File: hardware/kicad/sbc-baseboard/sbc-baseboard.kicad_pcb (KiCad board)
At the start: 6 copper layers, 140 x 100 mm, 339 parts, among them J1 USB-C upstream, J10 RJ45 magjack 10/100, J11 COM/NO/NC, J12 COM/NO/NC, J13 Console, J14 +5V_TGT out, J15 GPIO + I2C, J16 SWD, J17 Qwiic PD, J18 PSU in (isolated), J19 PSU out (isolated), J2 USB-C PD in, J3 USB-C HID to target, J4 USB-A x2, J5 USB-A x2, J601 SWD (K20), J9 FTDI header, K801 G6K-2F-Y DC5, K802 G6K-2F-Y DC5, K803 JW1FSN-DC5V, Q101 2N7002, Q102 2N7002, Q801 2N7002, Q802 2N7002, Q803 AO3400A, SW201 RESET, SW601 DAP RESET, U101 STUSB4500QTR, U102 PCA9517A, U103 TPS54560BDDA, U104 TPS54560BDDA, U105 TPS62823DLC, U201 MK64FN1M0VLL12, U202 USBLC6-2SC6, U301 KSZ8081RNA, U401 USBLC6-2SC6, U402 USB2517, U403 TPS2553DBV, U404 TPS2553DBV, U405 TPS2553DBV, U406 TPS2553DBV, U407 TPS2553DBV, U408 USBLC6-2SC6, U409 USBLC6-2SC6, U410 USBLC6-2SC6, U411 USBLC6-2SC6, U501 FT231XS, U601 MK20DX128VFM5, U701 TXB0104PW, U702 TXB0108PW, U703 TXS0102DCU, U704 TPS26630RGE, U801 LTV-817, Y201 32.768kHz, Y301 25MHz, Y401 24MHz, Y601 8MHz

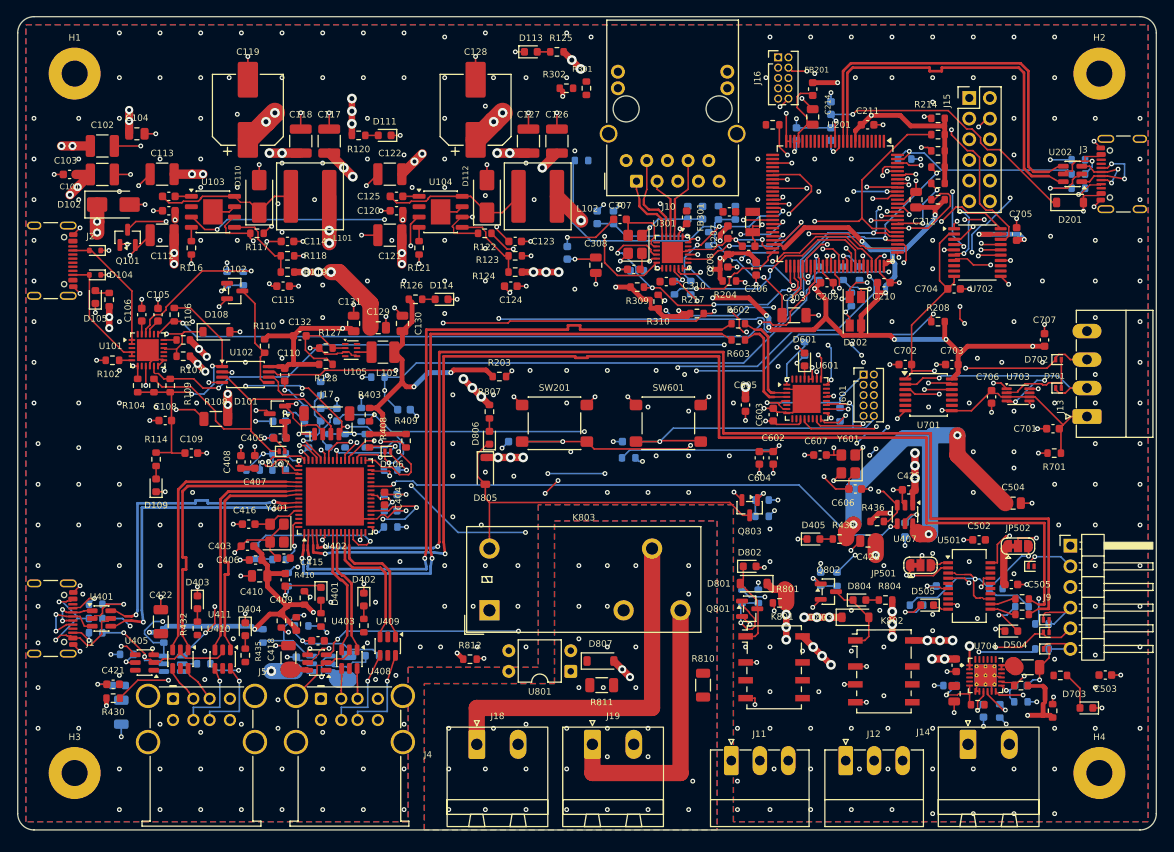
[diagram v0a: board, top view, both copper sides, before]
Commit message: The documents, the block diagram and the placed board for the barrel-jack inlet; 100 uF of bulk at the inlet
The specification (block diagram, connectors, parts, power tree and
budget at 20 W, pin budget, open questions, current pathways), the
README and the block diagram, the layout directives, guidelines and
reference-design review, the KiCad README and the protocol describe the
barrel inlet, the one +5V rail and the 3 A target rail; the PD inlet,
its controller, header and buffer and the two bucks remain as dated
history. A 100 uF electrolytic joins the two 47 uF at the inlet: the
hub's downstream ports want 120 uF on their rail, which buck 1's 194 uF
had given. Three older contradictions in the specification are settled
from the generator and the BOM: one FET per relay coil (2N7002 for the
signal relays, AO3400A for the power relay), the DAPLink on hub port 1,
the USB-A ports on hub ports 4 to 7. The board is committed placed and
unrouted (the route was stopped at the owner's request before it
finished): 271 parts, 480 connections, DRC clean.

Co-Authored-By: Claude Fable 5.1 <noreply@anthropic.com>
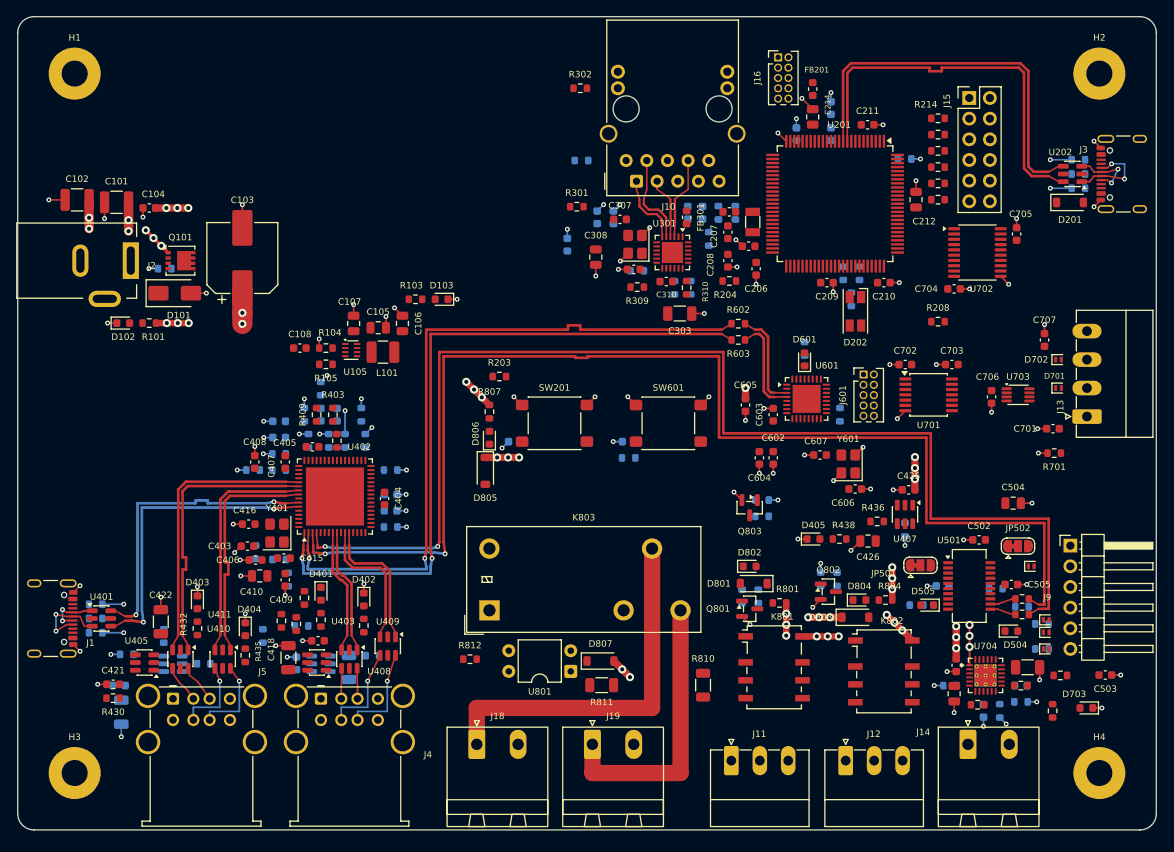
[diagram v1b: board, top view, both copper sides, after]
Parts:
- removed C109, C110: 100n, C_0603_1608Metric
- removed C111, C116: 100n/50V, C_0603_1608Metric
- removed C112, C113: 10u/50V, C_1210_3225Metric
- removed C114: 47p, C_0603_1608Metric
- removed C115: 4n7, C_0603_1608Metric
- removed C117, C118: 47u/10V, C_1210_3225Metric
- removed C119: 100u/10V, CP_Elec_8x10.5
- removed C129: 10u, C_0805_2012Metric
- removed C130, C131: 22u, C_0805_2012Metric
- removed C132: 120p, C_0603_1608Metric
- removed the C212 at (110.5, 22.5)
- removed the C213 at (95.8, 14.4)
- removed the C214 at (97.8, 12.3)
- removed the C301 at (82.4, 24.1)
- removed the C302 at (84.2, 24.1)
- removed the C303 at (95.5, 36.7)
- removed the C304 at (73.2, 24.7)
- removed the C305 at (71.2, 24.7)
- removed the C306 at (75.8, 31.1)
- removed D104: ESDA25W, D_SOD-523
- removed D105, D109, D111, D113, D114: LED AMBER, LED_0603_1608Metric
- removed D106, D107: PESD5V0S1UL, D_SOD-882
- removed D108: BZT52C5V1, D_SOD-123
- removed D110, D112: B560C, D_SMA
- removed the J15 at (117.0, 10.0)
- removed J17: Qwiic PD, JST_SH_BM04B-SRSS-TB_1x04-1MP_P1.00mm_Vertical
- removed the J3 at (136.9, 19.3)
- removed L102: 10u/6A, L_Coilcraft_XAL7020-102
- removed L103: 470n/4A, L_1210_3225Metric
- removed Q102: 2N7002, SOT-23
- removed R106, R109, R110: 10k, R_0603_1608Metric
- removed R107, R111, R112, R113, R115, R127: 100k, R_0603_1608Metric
- removed R108: 470, R_1206_3216Metric
- removed R114, R126: 470, R_0603_1608Metric
- removed R116, R121: 243k, R_0603_1608Metric
- removed R117, R122: 16.9k, R_0603_1608Metric
- removed R118, R123: 9.76k, R_0603_1608Metric
- removed R119, R124: 51.1k, R_0603_1608Metric
- removed R120, R125: 1k, R_0603_1608Metric
- removed R128: 453k, R_0603_1608Metric
- removed the R204 at (87.5, 32.5)
- removed R217, R218: 4.7k, R_0603_1608Metric
- removed the R307 at (80.8, 33.3)
- removed U101: STUSB4500QTR, QFN-24-1EP_4x4mm_P0.5mm_EP2.7x2.7mm
- removed U102: PCA9517A, TSSOP-8_4.4x3mm_P0.65mm
- removed U103, U104: TPS54560BDDA, HSOP-8-1EP_3.9x4.9mm_P1.27mm_EP2.41x3.1mm
- added D401: LED GREEN, LED_0603_1608Metric, F.Cu at (37.3, 71.0)
- added D805: 1N4148W, D_SOD-123, F.Cu at (57.5, 55.9)
- added J13: Console, PhoenixContact_MC_1,5_4-G-3.5_1x04_P3.50mm_Horizontal, F.Cu at (131.5, 49.2)
- added JP501: RTS/DTR, SolderJumper-3_P1.3mm_Bridged12_RoundedPad1.0x1.5mm, F.Cu at (111.0, 67.5)
- C101, C102: value 10u/50V -> 47u/10V
- C103: value 100n/50V -> 100u/10V; footprint C_0603_1608Metric -> CP_Elec_8x10.5
- C104: value 1u/50V -> 100n; footprint C_0805_2012Metric -> C_0603_1608Metric
- C105: value 1u -> 10u; footprint C_0603_1608Metric -> C_0805_2012Metric
- C106: value 1u -> 22u; footprint C_0603_1608Metric -> C_0805_2012Metric
- C107: value 1u -> 22u; footprint C_0603_1608Metric -> C_0805_2012Metric; moved to F.Cu
- C108: value 100n -> 120p
- C212: renamed from C120; value 100n/50V -> 10u; footprint C_0603_1608Metric -> C_0805_2012Metric
- C213: renamed from C121; value 10u/50V -> 100n; footprint C_1210_3225Metric -> C_0603_1608Metric; moved to B.Cu
- C214: renamed from C122; value 10u/50V -> 10u; footprint C_1210_3225Metric -> C_0805_2012Metric
- C301: renamed from C123; value 47p -> 100n; moved to B.Cu
- C302: renamed from C124; value 4n7 -> 100n; moved to B.Cu
- C303: renamed from C125; value 100n/50V -> 1n/2kV; footprint C_0603_1608Metric -> C_1206_3216Metric
- C304: renamed from C126; value 47u/10V -> 2u2; footprint C_1210_3225Metric -> C_0603_1608Metric; moved to B.Cu
- C305: renamed from C127; value 47u/10V -> 100n; footprint C_1210_3225Metric -> C_0603_1608Metric; moved to B.Cu
- C306: renamed from C128; value 100u/10V -> 22p; footprint CP_Elec_8x10.5 -> C_0603_1608Metric
- D101: value BAT54C -> SMAJ5.0A; footprint SOT-23 -> D_SMA
- D102: value SMAJ24A -> LED AMBER; footprint D_SMA -> LED_0603_1608Metric
- D103: value ESDA25W -> LED AMBER; footprint D_SOD-523 -> LED_0603_1608Metric
- J15: renamed from D805; value 1N4148W -> GPIO + I2C; footprint D_SOD-123 -> PinHeader_2x06_P2.54mm_Vertical
- J2: value USB-C PD in -> 5 V in, 2.5 mm; footprint USB_C_Receptacle_GCT_USB4105-xx-A_16P_TopMnt_Horizontal_PegClear -> BarrelJack_Kycon_KLDX-0202-xC_Horizontal
- J3: renamed from D401; value LED GREEN -> USB-C HID to target; footprint LED_0603_1608Metric -> USB_C_Receptacle_GCT_USB4105-xx-A_16P_TopMnt_Horizontal_PegClear
- L101: value 10u/6A -> 470n/4A; footprint L_Coilcraft_XAL7020-102 -> L_1210_3225Metric
- Q101: value 2N7002 -> DMP3013SFV; footprint SOT-23 -> Diodes_PowerDI3333-8
- R101: value 10k -> 1k
- R102: value 10k -> 100k; moved to B.Cu
- R103: value 1k -> 470
- R104: value 4.7k -> 100k
- R105: value 4.7k -> 453k
- R204: renamed from J13; value Console -> 10k; footprint PhoenixContact_MC_1,5_4-G-3.5_1x04_P3.50mm_Horizontal -> R_0603_1608Metric
- R307: renamed from JP501; value RTS/DTR -> 33; footprint SolderJumper-3_P1.3mm_Bridged12_RoundedPad1.0x1.5mm -> R_0603_1608Metric; moved to B.Cu
- R708: value 3.65k 1% -> 6.04k 1%
- moved J3 112.2 mm to (136.9, 19.3), turned to 90 degrees
- moved J15 75.1 mm to (117.0, 10.0), turned to 0 degrees
- moved C212 63.9 mm to (110.5, 22.5), turned to 90 degrees
- moved C214 52.5 mm to (97.8, 12.3), turned to 90 degrees
- moved C213 51.5 mm to (95.8, 14.4), turned to 90 degrees
- moved R204 47.0 mm to (87.5, 32.5), turned to 0 degrees
- moved R307 45.6 mm to (80.8, 33.3), turned to -90 degrees
- moved D103 43.0 mm to (52.1, 34.8)
- moved C303 37.7 mm to (81.4, 36.5), turned to 0 degrees
- moved C106 32.1 mm to (47.3, 37.7)
- moved R103 29.0 mm to (48.9, 34.8)
- moved C306 27.6 mm to (75.8, 31.1), turned to 180 degrees
- moved C105 27.1 mm to (44.3, 38.2), turned to 0 degrees
- moved C302 25.2 mm to (84.2, 24.1), turned to -90 degrees
- moved R104 23.6 mm to (37.9, 40.8), turned to 180 degrees
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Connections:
- net /Target I/O/+5V_TGT_OUT renamed /Target I/O/+5V_TGT
- C101 pad 1: VBUS_IN -> +5V
- C102 pad 1: VBUS_IN -> +5V
- C103 pad 1: VBUS_IN -> +5V
- C104 pad 1: VBUS_IN -> +5V
- C105 pad 1: Net-(U101-VREG_1V2) -> +5V
- C106 pad 1: Net-(U101-VREG_2V7) -> +3V3
- C107 pad 1: +3V3_PRG -> +3V3
- C108 pad 1: +3V3_PD -> +3V3
- C108 pad 2: GND -> Net-(U105-FB)
- C212 pad 1: VBUS_IN -> +3V3
- C213 pad 1: VBUS_IN -> +3V3A
- C214 pad 1: VBUS_IN -> +3V3A
- C301 pad 1: Net-(U104-COMP) -> Net-(J10-TCT)
- C302 pad 1: Net-(C124-Pad1) -> Net-(J10-RCT)
- C303 pad 1: Net-(U104-BOOT) -> Net-(C303-Pad1)
- C303 pad 2: Net-(D112-K) -> GND
- C304 pad 1: +5V_TGT -> Net-(U301-VDD_1.2)
- C305 pad 1: +5V_TGT -> Net-(U301-VDD_1.2)
- C306 pad 1: +5V_TGT -> Net-(U301-XO)
- C417 pad 1: +5V_PORTS -> +5V
- C419 pad 1: +5V_PORTS -> +5V
- C421 pad 1: +5V_PORTS -> +5V
- C423 pad 1: +5V_PORTS -> +5V
- C425 pad 1: +5V_PORTS -> +5V
- C605 pad 1: +5V_PORTS -> +5V
- C708 pad 1: +5V_TGT -> +5V
- C709 pad 1: +5V_TGT -> +5V
- D101 pad 1: +3V3 -> Net-(D101-K)
- D101 pad 2: +3V3_PRG -> GND
- D102 pad 1: VBUS_IN -> GND
- D102 pad 2: GND -> Net-(D102-A)
- D103 pad 2: Net-(D103-A2) -> Net-(D103-A)
- D801 pad 1: +5V_PORTS -> +5V
- D803 pad 1: +5V_PORTS -> +5V
- J15 pad 1: +5V_PORTS -> VREF_TGT
- J15 pad 2: Net-(D805-A) -> GND
- K801 pad 8: +5V_PORTS -> +5V
- K802 pad 8: +5V_PORTS -> +5V
- K803 pad 1: +5V_PORTS -> +5V
- L101 pad 1: Net-(D110-K) -> Net-(U105-SW)
- L101 pad 2: +5V_PORTS -> +3V3
- Q101 pad 1: /Power/PD_EN_GATE -> +5V
- Q101 pad 2: GND -> +5V
- Q101 pad 3: /Power/BUCK_EN -> +5V
- R101 pad 1: VBUS_IN -> +5V
- R101 pad 2: Net-(D105-A) -> Net-(D102-A)
- R102 pad 1: Net-(U101-RESET) -> Net-(Q101-G)
- R103 pad 1: Net-(U101-VBUS_VS_DISCH) -> +3V3
- R103 pad 2: VBUS_IN -> Net-(D103-A)
- R104 pad 1: +3V3_PD -> Net-(U105-FB)
- R104 pad 2: /Power/PD_SCL -> GND
- R105 pad 1: +3V3_PD -> +3V3
- R105 pad 2: /Power/PD_SDA -> Net-(U105-FB)
- R204 pad 1: VREF_TGT -> +3V3
- R204 pad 2: Net-(D701-K) -> Net-(U201-NMI_b/PTA4)
- R307 pad 1: Net-(JP501-A) -> Net-(U301-REF_CLK)
- R307 pad 2: Net-(JP501-C) -> RMII_CLK_50M
- R703 pad 1: +5V_TGT -> +5V
- R801 pad 1: +5V_PORTS -> +5V
- R804 pad 1: +5V_PORTS -> +5V
- R807 pad 1: +5V_PORTS -> +5V
- U105 pad 1: +5V_PORTS -> +5V
- U105 pad 7: +5V_PORTS -> +5V
- U201 pad 31: I2C0_SCL -> (no net)
- U201 pad 32: I2C0_SDA -> (no net)
- U201 pad 57: PD_ATTACH_N -> (no net)
- U201 pad 58: PD_ALERT_N -> (no net)
- U201 pad 59: PD_PROG_DET -> (no net)
- U403 pad 1: +5V_PORTS -> +5V
- U404 pad 1: +5V_PORTS -> +5V
- U405 pad 1: +5V_PORTS -> +5V
- U406 pad 1: +5V_PORTS -> +5V
- U407 pad 1: +5V_PORTS -> +5V
- U601 pad 6: +5V_PORTS -> +5V
- U704 pad 1: +5V_TGT -> +5V
- U704 pad 2: +5V_TGT -> +5V
- U704 pad 5: +5V_TGT -> +5V
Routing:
- net +3V3: track 496.1 -> 0.00 mm, vias 32 -> 0
- net GND: track 427.3 -> 152.9 mm, vias 459 -> 117
- net PORT3_FAULT_N: track 152.7 -> 0.00 mm, vias 6 -> 0
- net PORT4_FAULT_N: track 144.8 -> 0.00 mm, vias 4 -> 0
- net PORT2_FAULT_N: track 143.6 -> 0.00 mm, vias 7 -> 0
- net PORT3_EN: track 127.9 -> 0.00 mm, vias 7 -> 0
- net FTDI_FAULT_N: track 126.1 -> 0.00 mm, vias 4 -> 0
- net +3V3_PRG: track 120.1 -> 0.00 mm, vias 3 -> 0
- net PORT4_EN: track 119.9 -> 0.00 mm, vias 2 -> 0
- net PORT1_FAULT_N: track 116.8 -> 0.00 mm, vias 6 -> 0
- net PORT1_EN: track 113.7 -> 0.00 mm, vias 4 -> 0
- net K64_RESET_N: track 113.4 -> 0.00 mm, vias 8 -> 0
- net PORT2_EN: track 103.5 -> 0.00 mm, vias 3 -> 0
- net VREF_TGT: track 102.5 -> 0.00 mm, vias 2 -> 0
- net I2C0_SDA: track 95.8 -> 0.00 mm, vias 3 -> 0
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- added copper zone on In3.Cu, net +5V
- removed copper zone on In3.Cu, net +5V_PORTS
- removed copper zone on In3.Cu, net +5V_TGT
- removed copper zone on B.Cu, net GND
- removed copper zone on F.Cu, net GND
- removed copper zone on B.Cu, net PSU_GND
- removed copper zone on F.Cu, net PSU_GND
- removed copper zone on In3.Cu, net VBUS_IN

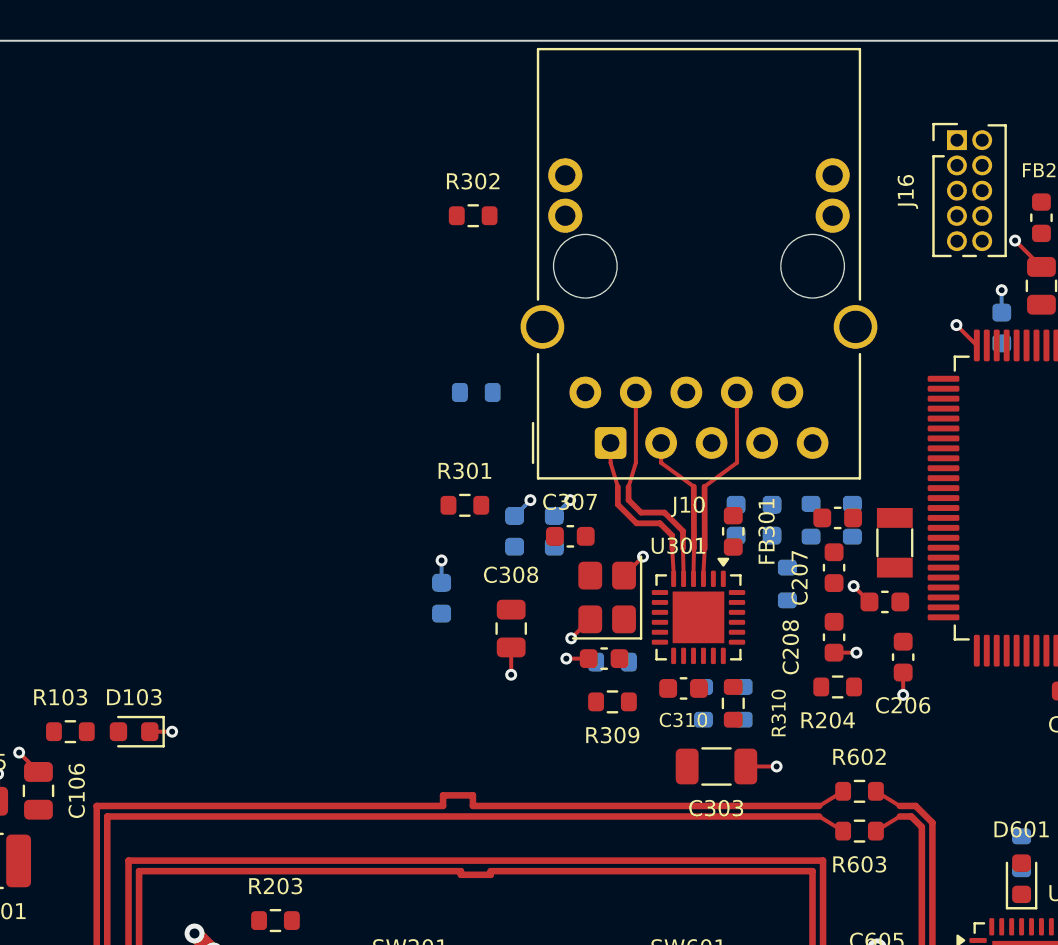
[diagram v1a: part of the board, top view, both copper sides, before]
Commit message: The RJ45 and its PHY 16 mm left along the back edge, into the corner the bucks left, opening the K64's side
J10 from x 71 to x 55, the PHY U301 with it so the Ethernet pairs keep
their 7 to 11 mm, the magnetics void following. The jack's body now ends
12 mm short of the K64's island and the PHY's parts 10 mm short of its
decoupling; the corner between the inlet and the jack (x 28 to 51) is
free. Placed and gated, unrouted: 479 connections, DRC clean.

Co-Authored-By: Claude Fable 5.1 <noreply@anthropic.com>
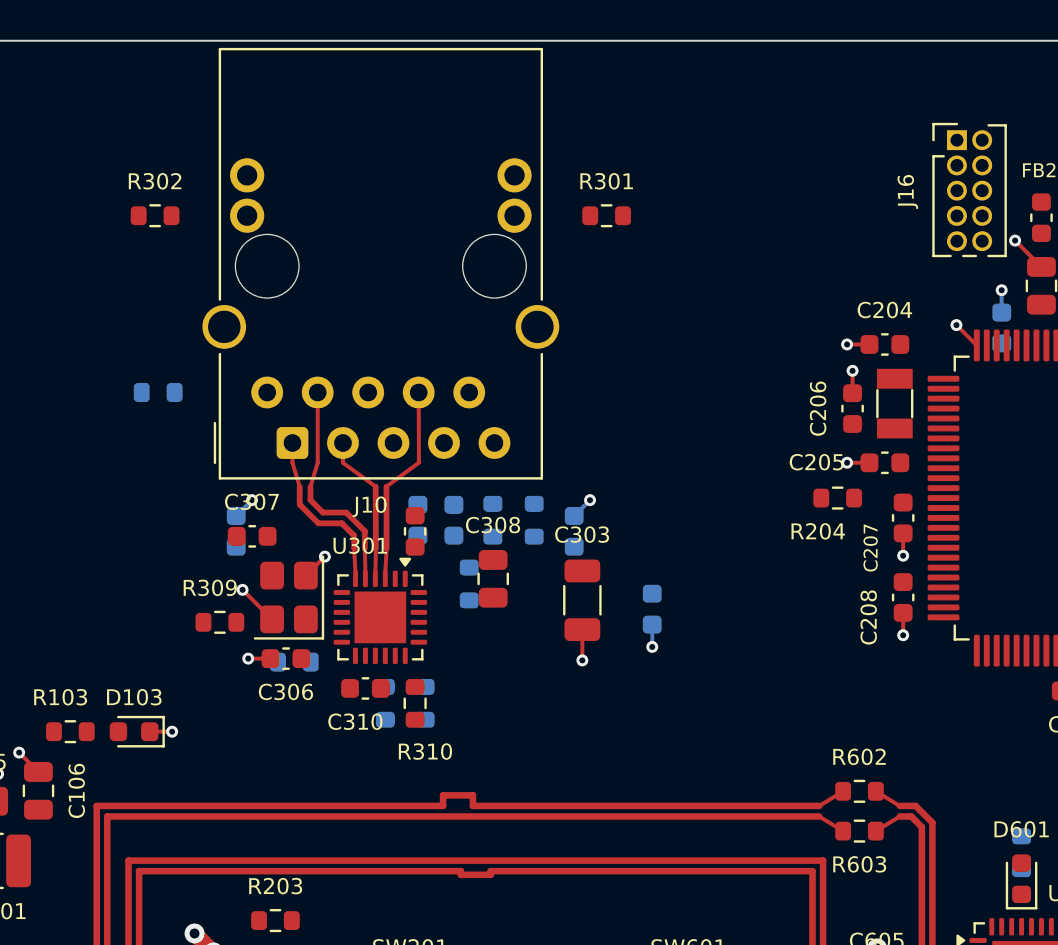
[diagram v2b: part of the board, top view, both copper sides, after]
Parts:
- moved R309 20.1 mm to (56.4, 29.2)
- moved R301 16.2 mm to (75.9, 8.80), turned to 0 degrees
- moved C307 16.0 mm to (58.1, 24.9)
- moved Y301 16.0 mm to (59.9, 28.0)
- moved C306 16.0 mm to (59.8, 31.1)
- moved C301 16.0 mm to (66.4, 24.1)
- moved C302 16.0 mm to (68.2, 24.1)
- moved C310 16.0 mm to (63.8, 32.6)
- moved FB301 16.0 mm to (66.2, 24.7)
- moved J10 16.0 mm to (60.1, 20.2)
- moved R302 16.0 mm to (53.2, 8.80)
- moved R303 16.0 mm to (70.2, 24.1)
- moved R304 16.0 mm to (69.0, 27.3)
- moved R305 16.0 mm to (72.2, 24.1)
- moved R307 16.0 mm to (64.8, 33.3)
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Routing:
- net GND: track 152.9 -> 154.6 mm, vias 117 -> 118

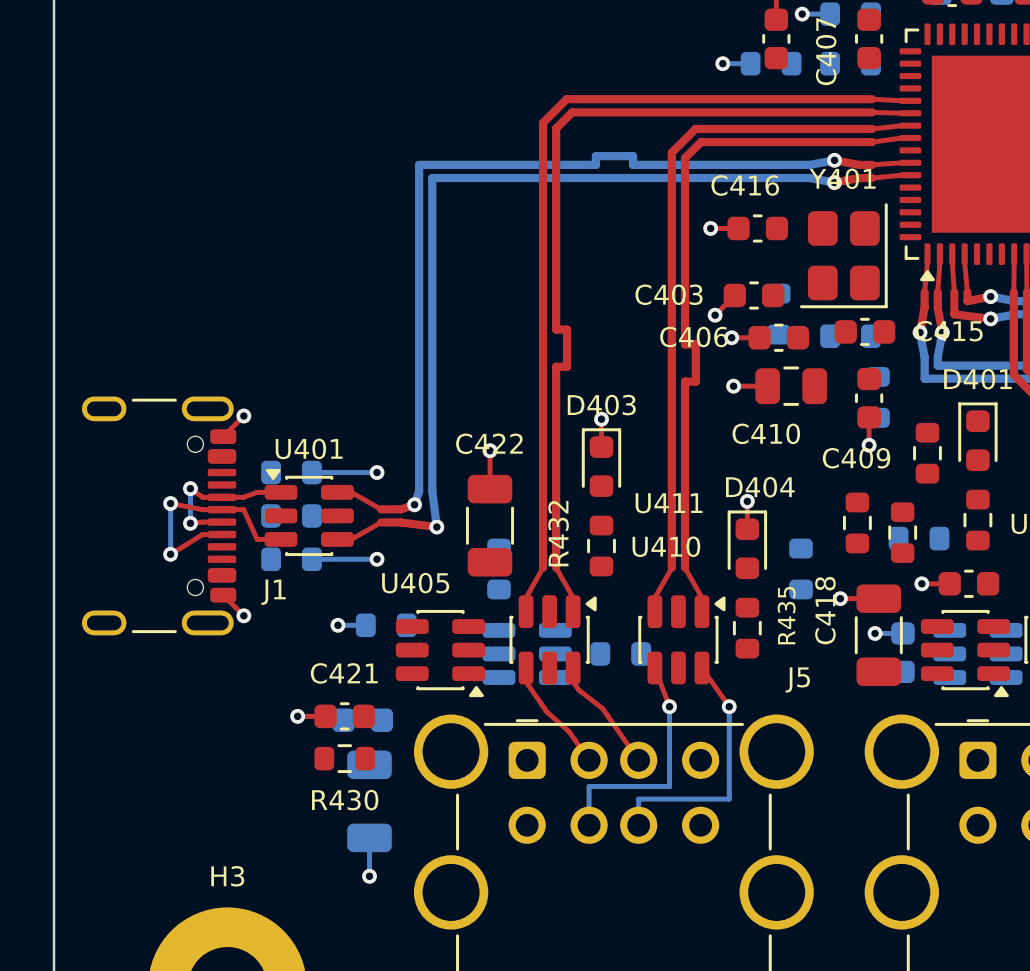
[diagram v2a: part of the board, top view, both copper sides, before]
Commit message: J1 10 mm up the left edge toward the middle, its ESD array with it
The upstream USB-C from y 74 to y 64; the hub's upstream pair lane goes
from 36.7 to 26.7 mm with the same two layer changes. Placed and gated,
unrouted: 479 connections, DRC clean.

Co-Authored-By: Claude Fable 5.1 <noreply@anthropic.com>
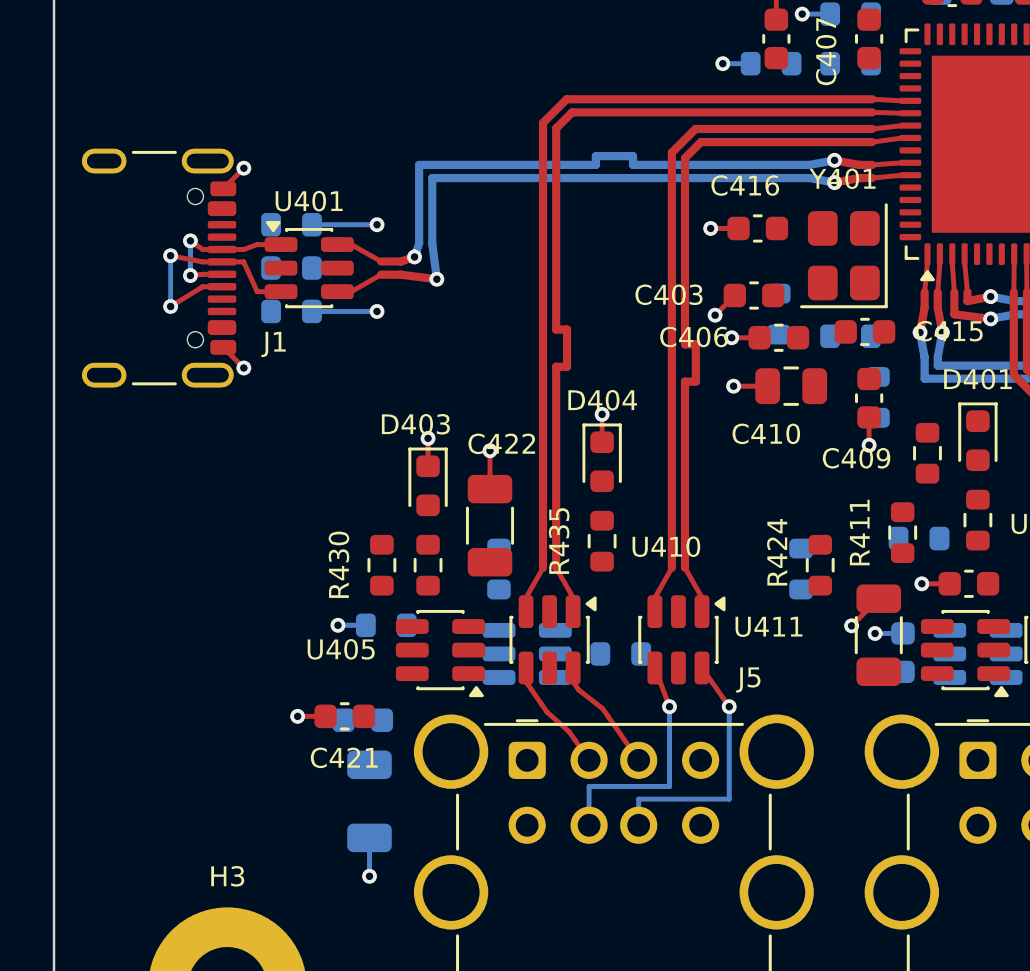
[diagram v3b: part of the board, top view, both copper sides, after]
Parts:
- moved J1 10.0 mm to (3.10, 64.0)
- moved R402 10.0 mm to (9.59, 64.0)
- moved R422 10.0 mm to (9.59, 62.2)
- moved R423 10.0 mm to (9.59, 65.8)
- moved U401 10.0 mm to (10.3, 64.0)
- moved R430 7.95 mm to (13.2, 76.0), turned to -90 degrees
- moved D403 7.04 mm to (15.1, 72.8)
- moved R432 7.04 mm to (15.1, 76.0)
- moved D404 6.83 mm to (22.1, 71.8)
- moved R435 6.83 mm to (22.1, 75.0)
- moved R424 2.27 mm to (30.9, 76.0)
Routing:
- net /USB hub/HUB_UP_P: track 36.7 -> 26.7 mm
- net /USB hub/HUB_UP_N: track 36.7 -> 26.7 mm
